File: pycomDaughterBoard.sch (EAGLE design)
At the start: 18 parts, among them J1 BilgeSwitch, J2 Button, J3 LED, J4 VCC

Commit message: new v0.3 board
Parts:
- removed DS18: DS18, SparkFun-Connectors:CONN_03-SCREW-5MM
- removed GPY, GPY1, GPY_II1: GPY, SparkFun-Connectors:CONN_14
- removed J1: BilgeSwitch, SparkFun-Retired:CONN_025MM
- removed J3: LED, SparkFun-Retired:CONN_025MM
- removed J4: VCC, SparkFun-Retired:CONN_025MM
- added 12, PY: RST, SparkFun-Connectors:CONN_14
- added HEADER: J1, SparkFun-Connectors:CONN_08"
- added VIN: GPY, SparkFun-Connectors:CONN_14
- J2: value Button -> VCC
- JST_5V: value JST_5V -> 5v
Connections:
- removed net N$19: GPY_II.6, GPY_II1.6
- removed net N$21: GPY_II.2, GPY_II1.2
- removed net N$22: GPY_II.1, GPY_II1.1
- removed net P12: GPY.12, GPY1.12, R7.2
- removed net P19: GPY_II.5, GPY_II1.5, J1.1
- new net 3V3: GPY_II.12, HEADER.5, HEADER.6, VIN.12
- new net N$12: GPY_II.9, VIN.9
- new net P13: GPY_II.1, HEADER.2, VIN.1
- new net P16: C1.1, GPY_II.4, R2.1, R3.2, VIN.4
- new net P17: GPY_II.5, VIN.5
- net 5V: now also JST_5V.2; no longer JST_5V.1
- net GND: now also HEADER.7, HEADER.8, J2.1, JST_5V.1, VIN.13; no longer DS18.3, GPY_II1.13, J1.2, J2.2, J3.2, J4.2, JST_5V.2
- net N$1: now also 12.1, PY.1; no longer GPY.1, GPY1.1
- net N$10: now also 12.9, PY.9; no longer GPY.13, GPY1.13
- net N$11: now also VIN.14; no longer GPY_II1.14
- net N$13: now also 12.10, PY.10; no longer GPY_II.12, GPY_II1.12
- net N$14: now also VIN.11; no longer GPY_II1.11
- net N$15: now also VIN.10; no longer GPY_II1.10
- net N$16: now also 12.14, PY.14; no longer GPY_II.9, GPY_II1.9
- net N$17: now also VIN.8; no longer GPY_II1.8
- net N$18: now also VIN.7; no longer GPY_II1.7
- net N$2: now also HEADER.1; no longer J3.1
- net N$20: now also VIN.3; no longer GPY_II1.3
- net N$3: now also 12.2, PY.2; no longer GPY.2, GPY1.2
- net N$4: now also 12.3, PY.3; no longer GPY.3, GPY1.3
- net N$5: now also 12.4, PY.4; no longer GPY.4, GPY1.4
- net N$6: now also 12.5, PY.5; no longer GPY.5, GPY1.5
- net N$7: now also 12.6, PY.6; no longer GPY.6, GPY1.6
- net N$8: now also 12.7, PY.7; no longer GPY.7, GPY1.7
- net N$9: now also 12.8, PY.8; no longer GPY.8, GPY1.8
- net P10: now also 12.12, PY.12, VCC.1; no longer DS18.2, GPY.10, GPY1.10
- net P11: now also 12.13, PY.13, R7.2; no longer GPY.11, GPY1.11, VCC.2
- net P14: now also GPY_II.2, HEADER.3, VIN.2; no longer GPY.14, GPY1.14, J2.1
- net P18: now also GPY_II.6, VIN.6; no longer C1.1, GPY_II.4, GPY_II1.4, R2.1, R3.2
- net P9: now also 12.11, HEADER.4, PY.11; no longer DS18.1, GPY.9, GPY1.9
- net VCC: now also J2.2, VCC.2; no longer J4.1, VCC.1
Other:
- note added: "Pycom Daughter Board External IO '''''''''''''''''''''''''''''''''''''''''''''''''''''''''''''''''''''''''''''''''' x = internal - no need for header P9 Input - Temp xP10 Output - VCC ENable P11 Output - LED P13 Input only - BilgeSwitch P14 Input only (pytrack) - Button xP16 Input only - VIN Voltage divider 2 Headers for GND - (LED, Temp) 1 Header for Temp power - (3V3_Sensors) 2 Headers for Bilg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"
- note removed: "Bilge Switch"
- note removed: "DS18B20"
- note removed: "LED Button"
- moved on the sheet: GPY_II, J2, JST_5V, R2, R7

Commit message: v0.4 of board, with JSR headers
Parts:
- removed HEADER: J1, SparkFun-Connectors:CONN_08"
- removed J2: VCC, SparkFun-Retired:CONN_025MM
- removed JST_5V: 5v, SparkFun-Connectors:CONN_02-JST-2-PTH-NO_SILK
- removed R7: 50, SparkFun-Resistors:1KOHM-HORIZ-1/4W-1%
- added JST_4RA: PERPHS, SparkFun-Connectors:CONN_04JST-PTH
- added JST_PWR: VVC_5V, SparkFun-Connectors:CONN_04JST-PTH
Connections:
- removed net N$2: HEADER.1, R7.1
- net 3V3: no longer HEADER.5, HEADER.6
- net 5V: now also JST_PWR.2; no longer JST_5V.2
- net GND: now also JST_4RA.3, JST_4RA.4, JST_PWR.1, JST_PWR.3; no longer HEADER.7, HEADER.8, J2.1, JST_5V.1
- net P11: no longer R7.2
- net P13: now also JST_4RA.1; no longer HEADER.2
- net P14: now also JST_4RA.2; no longer HEADER.3
- net P9: no longer HEADER.4
- net VCC: now also JST_PWR.4; no longer J2.2
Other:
- note added: "Pytrack External IO ''''''''''''''''''''''''''''''''''''''''''''' 1 GND DS18 GND 2 PWR_EN 3 3V3_Pymodule 4 3v3_Sensors DS18 VCC 5 P2 6 P9 DS18 DATA 7 P10 xOutpux VCC Enable 8 P11 Output LED 9 P4 10 P8 Pycom Daughter 4Pin JSTs ''''''''''''''''''''''''''''''''''''''''''''''''''''''''''''''' H1 P13 Input only - BilgeSwitch H2 P14 Input only (pytrack) - Button H3 GND - LED H4 GND - BilgeSwitch H1 GND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"
- note removed: "Pycom Daughter Board External IO '''''''''''''''''''''''''''''''''''''''''''''''''''''''''''''''''''''''''''''''''' x = internal - no need for header P9 Input - Temp xP10 Output - VCC ENable P11 Output - LED P13 Input only - BilgeSwitch P14 Input only (pytrack) - Button xP16 Input only - VIN Voltage divider 2 Headers for GND - (LED, Temp) 1 Header for Temp power - (3V3_Sensors) 2 Headers for Bilg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"
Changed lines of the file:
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@@
 <attributes>
 <attribute name="CNAME" value="pycom Daughter Board"/>
-<attribute name="CREVISION" value="0.3"/>
+<attribute name="CREVISION" value="0.4"/>
 <attribute name="DESIGNER" value="greg.cope@gmail.com"/>
 </attributes>
@@
 <part name="R3" library="SparkFun-Resistors" deviceset="1KOHM" device="-HORIZ-1/4W-1%" value="3.3M"/>
 <part name="R2" library="SparkFun-Resistors" deviceset="1KOHM" device="-HORIZ-1/4W-1%" value="27M"/>
-<part name="R7" library="SparkFun-Resistors" deviceset="1KOHM" device="-HORIZ-1/4W-1%" value="50"/>
 <part name="12" library="SparkFun-Connectors" deviceset="CONN_14" device="" value="RST"/>
 <part name="GPY_II" library="SparkFun-Connectors" deviceset="CONN_14" device="" value="GPY"/>
@@
 <part name="SUPPLY4" library="supply2" deviceset="GND" device=""/>
 <part name="SUPPLY3" library="supply2" deviceset="GND" device=""/>
-<part name="J2" library="SparkFun-Retired" deviceset="CONN_02" device="5MM" value="VCC"/>
-<part name="JST_5V" library="SparkFun-Connectors" deviceset="CONN_02" device="-JST-2-PTH-NO_SILK" value="5v"/>
-<part name="HEADER" library="SparkFun-Connectors" deviceset="CONN_08" device="&quot;" value="J1"/>
+<part name="JST_PWR" library="SparkFun-Connectors" deviceset="CONN_04" device="JST-PTH" value="VVC_5V"/>
+<part name="JST_4RA" library="SparkFun-Connectors" deviceset="CONN_04" device="JST-PTH" value="PERPHS"/>
+<part name="SUPPLY5" library="supply2" deviceset="GND" device=""/>
 </parts>
 <sheets>
@@
 5V Output
 Max 600mA, 96% eff</text>
-<text x="137.16" y="30.48" size="3.81" layer="91">Pycom Daughter Board External IO
-''''''''''''''''''''''''''''''''''''''''''''''''''''''''''''''''''''''''''''''''''
+<text x="160.02" y="22.86" size="3.81" layer="91">Pytrack External IO
+'''''''''''''''''''''''''''''''''''''''''''''
+1 GND                    DS18 GND
+2 PWR_EN
+3 3V3_Pymodule
+4 3v3_Sensors       DS18 VCC
+5 P2
+6 P9                        DS18 DATA
+7 P10                      xOutpux VCC Enable
+8 P11                      Output LED
+9 P4
+10 P8
+Pycom Daughter 4Pin JSTs
+'''''''''''''''''''''''''''''''''''''''''''''''''''''''''''''''
+H1 P13 Input only - BilgeSwitch
+H2 P14 Input only (pytrack) - Button
+H3 GND - LED
+H4 GND - BilgeSwitch
+H1 GND 5V rail
+H2 5V
+H3 GND VCC rail
+H4 VCC
 x = internal - no need for header
-P9 Input - Temp
-xP10 Output - VCC ENable
-P11 Output - LED
-P13 Input only - BilgeSwitch
-P14 Input only (pytrack) - Button
-xP16 Input only - VIN Voltage divider
-2 Headers for GND - (LED, Temp)
-1 Header for Temp power - (3V3_Sensors)
-2 Headers for Bilge &amp; Button - (3v3)</text>
+</text>
 </plain>
 <instances>
@@
 <instance part="R3" gate="G$1" x="50.8" y="144.78" rot="R90"/>
 <instance part="R2" gate="G$1" x="50.8" y="157.48" rot="R90"/>
-<instance part="R7" gate="G$1" x="55.88" y="73.66"/>
 <instance part="12" gate="G$1" x="63.5" y="35.56" smashed="yes" rot="R180">
 <attribute name="VALUE" x="63.5" y="58.166" size="1.778" layer="96" font="vector" rot="R180"/>
@@
 </instance>
 <instance part="VIN" gate="G$1" x="78.74" y="38.1"/>
-<instance part="SUPPLY4" gate="GND" x="63.5" y="88.9"/>
+<instance part="SUPPLY4" gate="GND" x="50.8" y="91.44"/>
 <instance part="SUPPLY3" gate="GND" x="116.84" y="48.26"/>
-<instance part="J2" gate="G$1" x="17.78" y="139.7"/>
-<instance part="JST_5V" gate="G$1" x="139.7" y="149.86"/>
-<instance part="HEADER" gate="G$1" x="33.02" y="81.28"/>
+<instance part="JST_PWR" gate="G$1" x="20.32" y="137.16"/>
+<instance part="JST_4RA" gate="G$1" x="20.32" y="88.9"/>
+<instance part="SUPPLY5" gate="GND" x="33.02" y="132.08"/>
 </instances>
 <busses>
@@
 <wire x1="96.52" y1="137.16" x2="96.52" y2="139.7" width="0.1524" layer="91"/>
 <junction x="96.52" y="139.7"/>
-<pinref part="J2" gate="G$1" pin="1"/>
+<pinref part="JST_PWR" gate="G$1" pin="3"/>
 </segment>
 <segment>
@@
 <label x="129.54" y="139.7" size="1.778" layer="95"/>
 <pinref part="SUPPLY1" gate="GND" pin="GND"/>
-<wire x1="147.32" y1="149.86" x2="147.32" y2="139.7" width="0.1524" layer="91"/>
-<wire x1="147.32" y1="139.7" x2="134.62" y2="139.7" width="0.1524" layer="91"/>
-<junction x="134.62" y="139.7"/>
-<pinref part="JST_5V" gate="G$1" pin="1"/>
 </segment>
 <segment>
@@
 </segment>
 <segment>
+<pinref part="JST_PWR" gate="G$1" pin="1"/>
+<wire x1="25.4" y1="134.62" x2="33.02" y2="134.62" width="0.1524" layer="91"/>
+<pinref part="SUPPLY5" gate="GND" pin="GND"/>
+</segment>
+<segment>
+<pinref part="JST_4RA" gate="G$1" pin="4"/>
 <pinref part="SUPPLY4" gate="GND" pin="GND"/>
-<label x="38.1" y="91.44" size="1.778" layer="95"/>
-<pinref part="HEADER" gate="G$1" pin="7"/>
-<wire x1="53.34" y1="91.44" x2="63.5" y2="91.44" width="0.1524" layer="91"/>
-<wire x1="38.1" y1="88.9" x2="53.34" y2="88.9" width="0.1524" layer="91"/>
-<wire x1="53.34" y1="88.9" x2="53.34" y2="91.44" width="0.1524" layer="91"/>
-<label x="38.1" y="88.9" size="1.778" layer="95"/>
-<pinref part="HEADER" gate="G$1" pin="8"/>
-<wire x1="38.1" y1="91.44" x2="53.34" y2="91.44" width="0.1524" layer="91"/>
-<junction x="53.34" y="91.44"/>
+<wire x1="25.4" y1="93.98" x2="40.64" y2="93.98" width="0.1524" layer="91"/>
+<pinref part="JST_4RA" gate="G$1" pin="3"/>
+<wire x1="40.64" y1="93.98" x2="50.8" y2="93.98" width="0.1524" layer="91"/>
+<wire x1="25.4" y1="91.44" x2="40.64" y2="91.44" width="0.1524" layer="91"/>
+<wire x1="40.64" y1="91.44" x2="40.64" y2="93.98" width="0.1524" layer="91"/>
+<junction x="40.64" y="93.98"/>
+<label x="25.4" y="91.44" size="1.778" layer="95"/>
+<label x="25.4" y="93.98" size="1.778" layer="95"/>
 </segment>
 </net>
@@
 <wire x1="50.8" y1="162.56" x2="96.52" y2="162.56" width="0.1524" layer="91"/>
 <junction x="50.8" y="162.56"/>
-<pinref part="J2" gate="G$1" pin="2"/>
+<pinref part="JST_PWR" gate="G$1" pin="4"/>
 </segment>
 </net>
@@
 <pinref part="5V" gate="G$1" pin="2"/>
 <wire x1="127" y1="162.56" x2="127" y2="165.1" width="0.1524" layer="91"/>
+<label x="129.54" y="165.1" size="1.778" layer="95"/>
 <wire x1="127" y1="165.1" x2="147.32" y2="165.1" width="0.1524" layer="91"/>
 <junction x="127" y="165.1"/>
-<label x="129.54" y="165.1" size="1.778" layer="95"/>
-<wire x1="147.32" y1="165.1" x2="147.32" y2="152.4" width="0.1524" layer="91"/>
-<pinref part="JST_5V" gate="G$1" pin="2"/>
+<wire x1="147.32" y1="165.1" x2="147.32" y2="127" width="0.1524" layer="91"/>
+<wire x1="147.32" y1="127" x2="43.18" y2="127" width="0.1524" layer="91"/>
+<wire x1="43.18" y1="127" x2="43.18" y2="137.16" width="0.1524" layer="91"/>
+<pinref part="JST_PWR" gate="G$1" pin="2"/>
+<wire x1="43.18" y1="137.16" x2="25.4" y2="137.16" width="0.1524" layer="91"/>
 </segment>
 </net>
@@
 <junction x="53.34" y="27.94"/>
 </segment>
-<segment>
-<wire x1="38.1" y1="81.28" x2="53.34" y2="81.28" width="0.1524" layer="91"/>
-<label x="38.1" y="81.28" size="1.778" layer="95"/>
-<pinref part="HEADER" gate="G$1" pin="4"/>
-</segment>
 </net>
 <net name="P10" class="1">
@@
 <label x="43.18" y="22.86" size="1.778" layer="95"/>
 </segment>
-<segment>
-<pinref part="R7" gate="G$1" pin="2"/>
-<wire x1="60.96" y1="73.66" x2="66.04" y2="73.66" width="0.1524" layer="91"/>
-<label x="60.96" y="73.66" size="1.778" layer="95"/>
-</segment>
 </net>
 <net name="P14" class="1">
@@
 </segment>
 <segment>
-<wire x1="38.1" y1="78.74" x2="53.34" y2="78.74" width="0.1524" layer="91"/>
-<label x="38.1" y="78.74" size="1.778" layer="95"/>
-<pinref part="HEADER" gate="G$1" pin="3"/>
+<pinref part="JST_4RA" gate="G$1" pin="2"/>
+<wire x1="25.4" y1="88.9" x2="40.64" y2="88.9" width="0.1524" layer="91"/>
+<label x="25.4" y="88.9" size="1.778" layer="95"/>
 </segment>
 </net>
@@
 <label x="106.68" y="48.26" size="1.778" layer="95"/>
 </segment>
-<segment>
-<wire x1="38.1" y1="86.36" x2="53.34" y2="86.36" width="0.1524" layer="91"/>
-<label x="38.1" y="86.36" size="1.778" layer="95"/>
-<pinref part="HEADER" gate="G$1" pin="6"/>
-</segment>
-<segment>
-<wire x1="38.1" y1="83.82" x2="53.34" y2="83.82" width="0.1524" layer="91"/>
-<label x="38.1" y="83.82" size="1.778" layer="95"/>
-<pinref part="HEADER" gate="G$1" pin="5"/>
-</segment>
 </net>
 <net name="N$14" class="1">
@@
 </segment>
 <segment>
-<wire x1="53.34" y1="76.2" x2="38.1" y2="76.2" width="0.1524" layer="91"/>
-<label x="38.1" y="76.2" size="1.778" layer="95"/>
-<pinref part="HEADER" gate="G$1" pin="2"/>
+<pinref part="JST_4RA" gate="G$1" pin="1"/>
+<wire x1="25.4" y1="86.36" x2="40.64" y2="86.36" width="0.1524" layer="91"/>
+<label x="25.4" y="86.36" size="1.778" layer="95"/>
 </segment>
 </net>
@@
 </segment>
 </net>
-<net name="N$2" class="1">
-<segment>
-<pinref part="R7" gate="G$1" pin="1"/>
-<wire x1="38.1" y1="73.66" x2="50.8" y2="73.66" width="0.1524" layer="91"/>
-<pinref part="HEADER" gate="G$1" pin="1"/>
-</segment>
-</net>

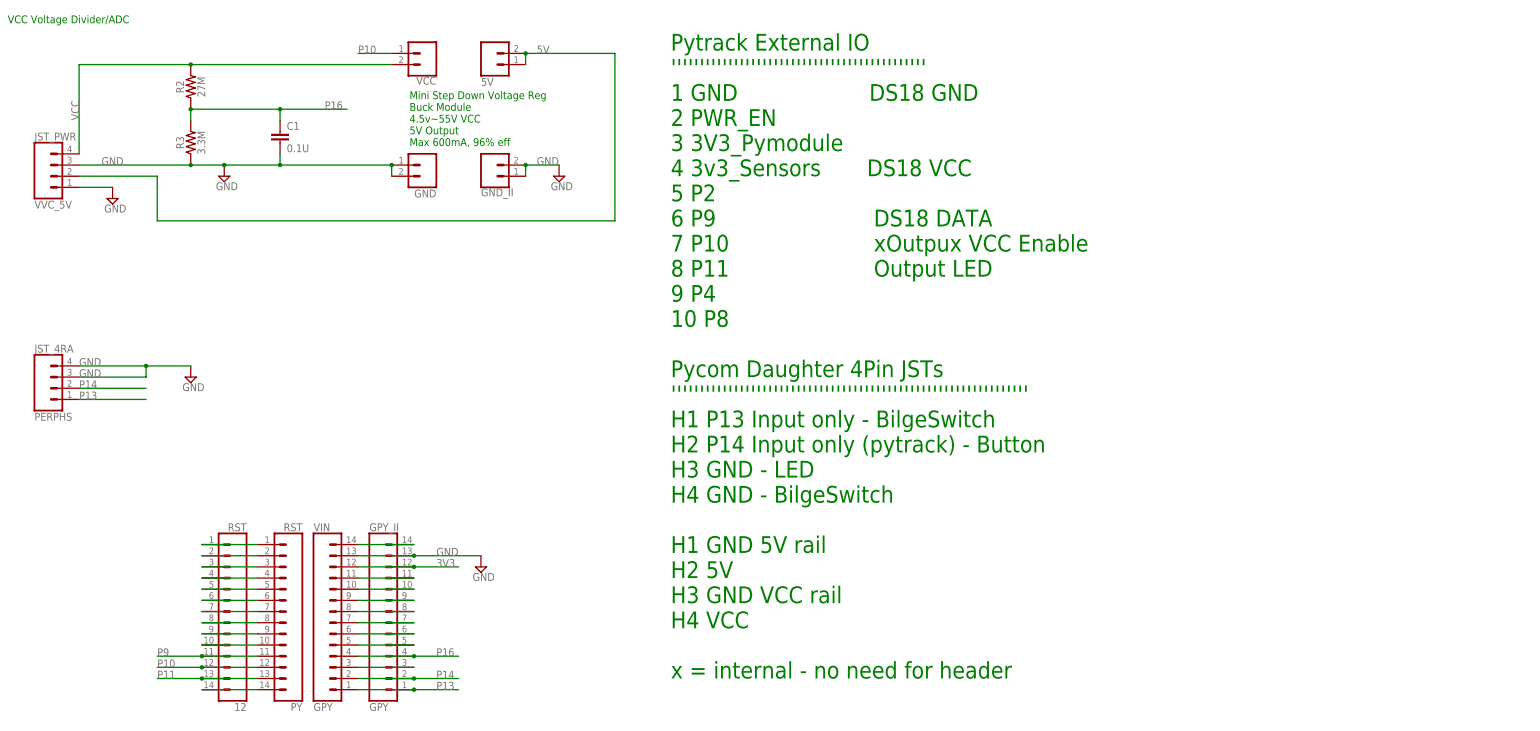
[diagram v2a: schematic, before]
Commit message: Board v0.6 updates
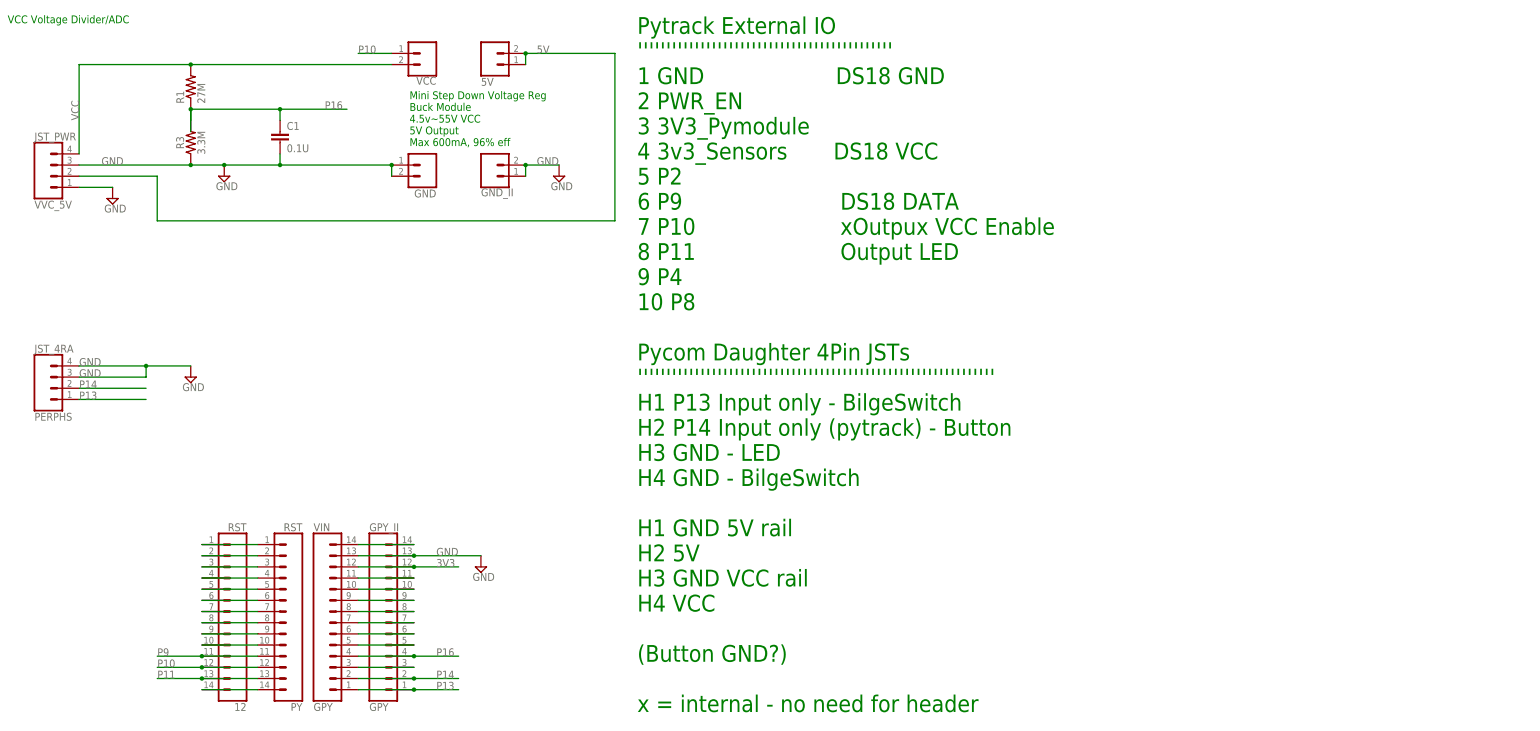
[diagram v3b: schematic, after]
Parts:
- removed R2: 27M, SparkFun-Resistors:1KOHM-HORIZ-1/4W-1%
- added R1: 27M, adafruit:R-US_0309/12
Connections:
- net P16: now also R1.1; no longer R2.1
- net VCC: now also R1.2; no longer R2.2
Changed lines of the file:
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@@
 <attributes>
 <attribute name="CNAME" value="pycom Daughter Board"/>
-<attribute name="CREVISION" value="0.4"/>
+<attribute name="CREVISION" value="0.5"/>
 <attribute name="DESIGNER" value="greg.cope@gmail.com"/>
 </attributes>
@@
 <part name="C1" library="SparkFun-Capacitors" deviceset="0.1UF" device="-KIT-EZ-50V-20%" value="0.1U"/>
 <part name="R3" library="SparkFun-Resistors" deviceset="1KOHM" device="-HORIZ-1/4W-1%" value="3.3M"/>
-<part name="R2" library="SparkFun-Resistors" deviceset="1KOHM" device="-HORIZ-1/4W-1%" value="27M"/>
 <part name="12" library="SparkFun-Connectors" deviceset="CONN_14" device="" value="RST"/>
 <part name="GPY_II" library="SparkFun-Connectors" deviceset="CONN_14" device="" value="GPY"/>
@@
 <part name="JST_4RA" library="SparkFun-Connectors" deviceset="CONN_04" device="JST-PTH" value="PERPHS"/>
 <part name="SUPPLY5" library="supply2" deviceset="GND" device=""/>
+<part name="R1" library="adafruit" deviceset="R-US_" device="0309/12" value="27M"/>
 </parts>
 <sheets>
@@
 5V Output
 Max 600mA, 96% eff</text>
-<text x="160.02" y="22.86" size="3.81" layer="91">Pytrack External IO
+<text x="152.4" y="15.24" size="3.81" layer="91">Pytrack External IO
 '''''''''''''''''''''''''''''''''''''''''''''
 1 GND                    DS18 GND
@@
 H3 GND VCC rail
 H4 VCC
+(Button GND?)
 x = internal - no need for header
 </text>
@@
 <instance part="C1" gate="G$1" x="71.12" y="144.78"/>
 <instance part="R3" gate="G$1" x="50.8" y="144.78" rot="R90"/>
-<instance part="R2" gate="G$1" x="50.8" y="157.48" rot="R90"/>
 <instance part="12" gate="G$1" x="63.5" y="35.56" smashed="yes" rot="R180">
 <attribute name="VALUE" x="63.5" y="58.166" size="1.778" layer="96" font="vector" rot="R180"/>
@@
 <instance part="JST_4RA" gate="G$1" x="20.32" y="88.9"/>
 <instance part="SUPPLY5" gate="GND" x="33.02" y="132.08"/>
+<instance part="R1" gate="G$1" x="50.8" y="157.48" rot="R90"/>
 </instances>
 <busses>
@@
 <net name="VCC" class="1">
 <segment>
-<wire x1="50.8" y1="162.56" x2="25.4" y2="162.56" width="0.1524" layer="91"/>
 <wire x1="25.4" y1="162.56" x2="25.4" y2="142.24" width="0.1524" layer="91"/>
 <label x="25.4" y="149.86" size="1.778" layer="95" rot="R90"/>
-<pinref part="R2" gate="G$1" pin="2"/>
 <pinref part="VCC" gate="G$1" pin="2"/>
+<pinref part="JST_PWR" gate="G$1" pin="4"/>
+<wire x1="25.4" y1="162.56" x2="50.8" y2="162.56" width="0.1524" layer="91"/>
+<pinref part="R1" gate="G$1" pin="2"/>
 <wire x1="50.8" y1="162.56" x2="96.52" y2="162.56" width="0.1524" layer="91"/>
 <junction x="50.8" y="162.56"/>
-<pinref part="JST_PWR" gate="G$1" pin="4"/>
 </segment>
 </net>
@@
 <segment>
 <pinref part="C1" gate="G$1" pin="1"/>
-<pinref part="R2" gate="G$1" pin="1"/>
 <pinref part="R3" gate="G$1" pin="2"/>
-<wire x1="50.8" y1="152.4" x2="50.8" y2="149.86" width="0.1524" layer="91"/>
 <wire x1="71.12" y1="149.86" x2="71.12" y2="152.4" width="0.1524" layer="91"/>
 <wire x1="71.12" y1="152.4" x2="50.8" y2="152.4" width="0.1524" layer="91"/>
-<junction x="50.8" y="152.4"/>
 <wire x1="71.12" y1="152.4" x2="86.36" y2="152.4" width="0.1524" layer="91"/>
 <junction x="71.12" y="152.4"/>
 <label x="81.28" y="152.4" size="1.778" layer="95"/>
-</segment>
-</net>
+<junction x="50.8" y="152.4"/>
+<wire x1="50.8" y1="152.4" x2="50.8" y2="149.86" width="0.1524" layer="91"/>
+<wire x1="50.8" y1="147.32" x2="50.8" y2="152.4" width="0.1524" layer="91"/>
+<pinref part="R1" gate="G$1" pin="1"/>
+</segment>
+</net>
